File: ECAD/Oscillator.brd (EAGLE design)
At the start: 86 x 43.5 mm, 18 parts

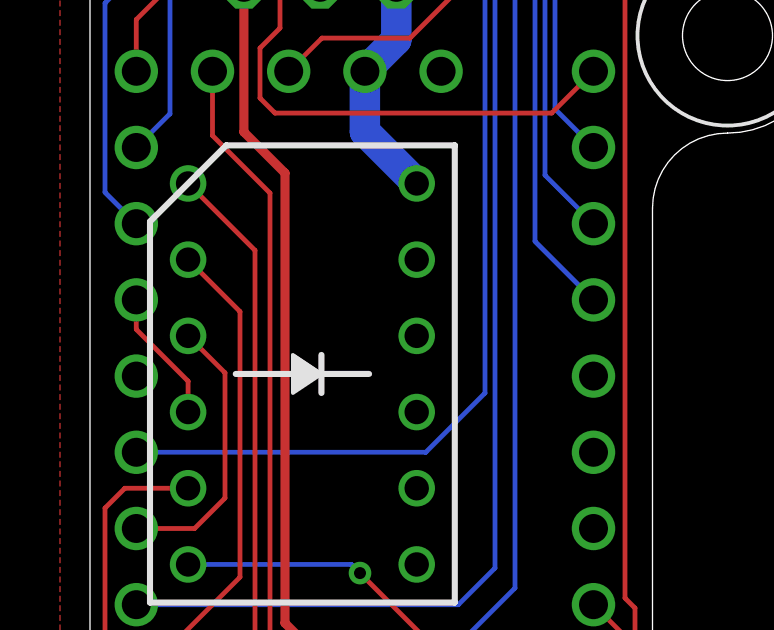
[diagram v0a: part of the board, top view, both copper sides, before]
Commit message: Moved the LED bar graphs' color labels to the silkscreen layer.
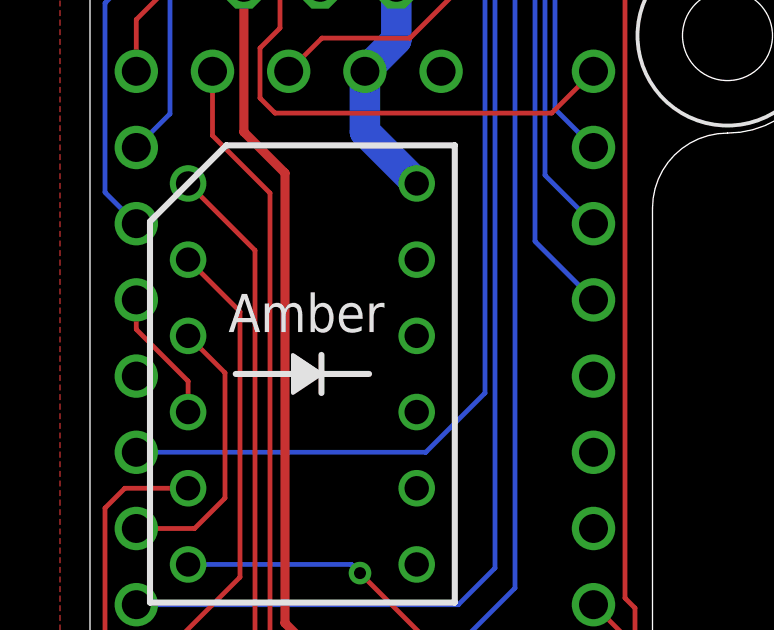
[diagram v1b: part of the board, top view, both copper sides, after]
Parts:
- D1: value Red -> Amber
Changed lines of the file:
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@@
 </autorouter>
 <elements>
-<element name="D1" library="SynthLib" package="LED_BARGRAPH_6" value="Red" x="7.08" y="25.471" smashed="yes" rot="R270">
-<attribute name="VALUE" x="5.611665625" y="26.867665625" size="1.27" layer="27"/>
+<element name="D1" library="SynthLib" package="LED_BARGRAPH_6" value="Amber" x="7.08" y="25.471" smashed="yes" rot="R270">
+<attribute name="VALUE" x="4.611665625" y="26.867665625" size="1.27" layer="21"/>
 </element>
 <element name="JP1" library="jumper" package="JP3Q" value="SPI_POWER" x="7.67" y="39.603334375" smashed="yes" rot="MR180"/>
